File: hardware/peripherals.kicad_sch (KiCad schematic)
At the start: 40 parts, among them J2 Conn_FSR_TopRight, J3 Conn_FSR_BotRight, J4 Conn_FSR_TopLeft, J5 Conn_FSR_BotLeft, U2 BNO055, Y1 32.768k

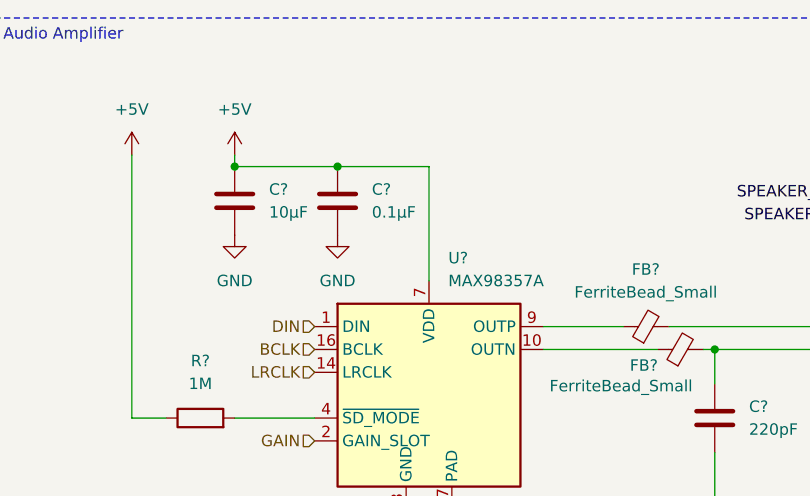
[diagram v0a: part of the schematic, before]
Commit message: Adding LED datasheet
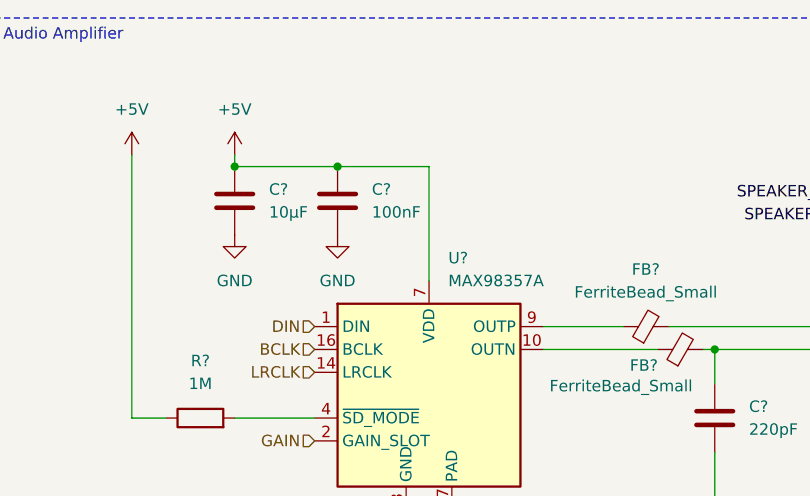
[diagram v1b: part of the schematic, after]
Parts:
- C?: value 0.1µF -> 100nF
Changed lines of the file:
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@@
 			)
 		)
-		(property "Value" "0.1µF"
+		(property "Value" "100nF"
 			(at 55.88 36.8299 0)
 			(effects
@@
 			)
 		)
-		(property "Datasheet" "https://cdn-shop.adafruit.com/product-files/1138/SK6812+LED+datasheet+.pdf"
+		(property "Datasheet" "https://github.com/Mowibox/chromapi_motherboard/blob/main/docs/datasheets/SK6812+LED+datasheet+.pdf"
 			(at 162.56 155.575 0)
 			(effects
@@
 			)
 		)
-		(property "Datasheet" "https://cdn-shop.adafruit.com/product-files/1138/SK6812+LED+datasheet+.pdf"
+		(property "Datasheet" "https://github.com/Mowibox/chromapi_motherboard/blob/main/docs/datasheets/SK6812+LED+datasheet+.pdf"
 			(at 162.56 120.015 0)
 			(effects

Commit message: Schematic first draft
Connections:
- net GAIN is gone; now on net GND: U?.2 (GAIN_SLOT)
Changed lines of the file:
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@@
 	(wire
 		(pts
+			(xy 49.53 62.23) (xy 48.26 62.23)
+		)
+		(stroke
+			(width 0)
+			(type default)
+		)
+	)
+	(wire
+		(pts
 			(xy 78.74 102.87) (xy 73.66 102.87)
 		)
@@
 	(wire
 		(pts
+			(xy 48.26 62.23) (xy 48.26 69.85)
+		)
+		(stroke
+			(width 0)
+			(type default)
+		)
+	)
+	(wire
+		(pts
 			(xy 199.39 97.79) (xy 199.39 102.87)
 		)
@@
 		)
 	)
-	(hierarchical_label "GAIN"
-		(shape input)
-		(at 49.53 62.23 180)
-		(effects
-			(font
-				(size 1.27 1.27)
-			)
-			(justify right)
-		)
-	)
 	(hierarchical_label "FSR_BotLeft"
 		(shape input)
@@
 					(unit 1)
 				)
+			)
+		)
+	)
+	(symbol
+		(lib_id "power:GND")
+		(at 48.26 69.85 0)
+		(unit 1)
+		(exclude_from_sim no)
+		(in_bom yes)
+		(on_board yes)
+		(dnp no)
+		(fields_autoplaced yes)
+		(property "Reference" "#PWR0105"
+			(at 48.26 76.2 0)
+			(effects
+				(font
+					(size 1.27 1.27)
+				)
+				(hide yes)
+			)
+		)
+		(property "Value" "GND"
+			(at 48.26 74.93 0)
+			(effects
+				(font
+					(size 1.27 1.27)
+				)
+			)
+		)
+		(property "Footprint" ""
+			(at 48.26 69.85 0)
+			(effects
+				(font
+					(size 1.27 1.27)
+				)
+				(hide yes)
+			)
+		)
+		(property "Datasheet" ""
+			(at 48.26 69.85 0)
+			(effects
+				(font
+					(size 1.27 1.27)
+				)
+				(hide yes)
+			)
+		)
+		(property "Description" "Power symbol creates a global label with name \"GND\" , ground"
+			(at 48.26 69.85 0)
+			(effects
+				(font
+					(size 1.27 1.27)
+				)
+				(hide yes)
+			)
+		)
+		(pin "1"
+		)
+		(instances
+			(project "chromapi_motherboard_v1"
+				(path "/d1a31f26-03e0-43e1-89c1-031fe31befc5/e7c408c3-7bc5-47c0-a90d-18a385ee9c4c"
+					(reference "#PWR0105")
+					(unit 1)
+				)

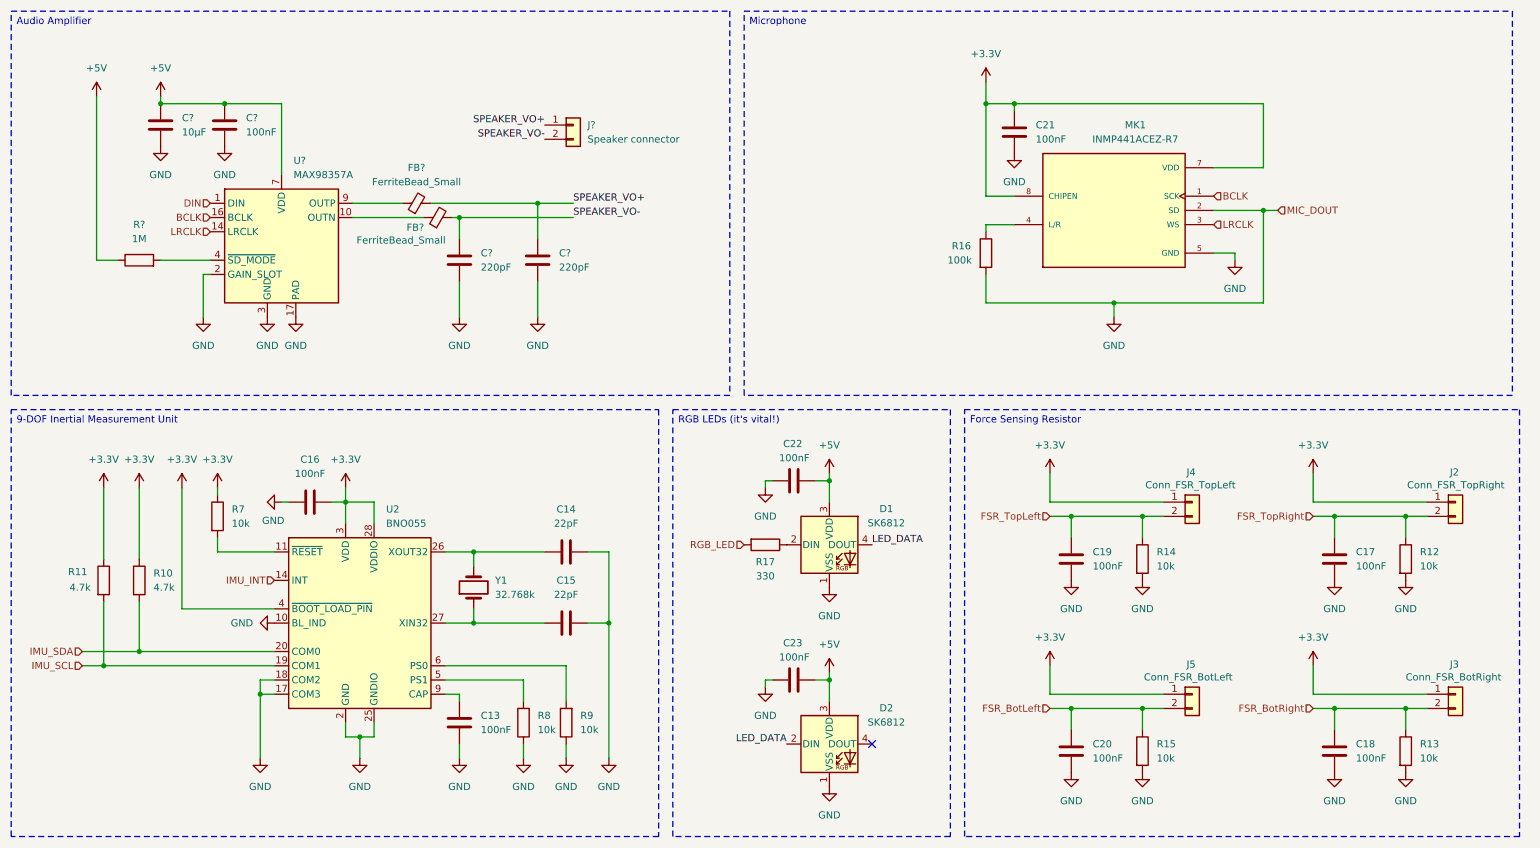
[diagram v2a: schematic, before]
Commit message: Annotating schematic
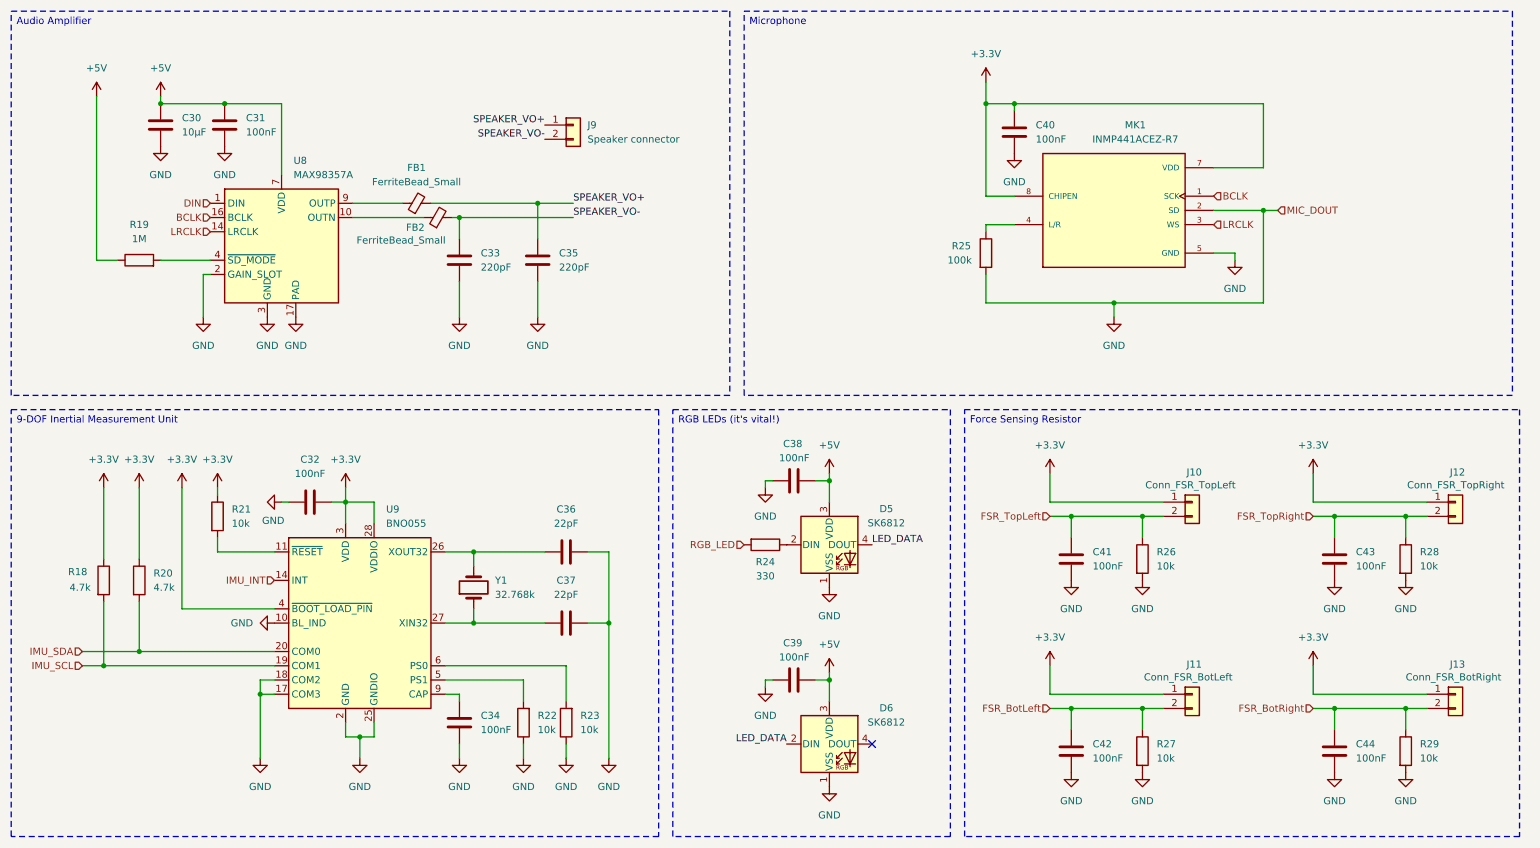
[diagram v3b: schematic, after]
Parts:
- gave numbers to parts that had none: 9
- renumbered C16 to C32, C13 to C34, C14 to C36, C15 to C37, C22 to C38, C23 to C39, C21 to C40, C19 to C41, C20 to C42, C17 to C43, C18 to C44, D1 to D5, D2 to D6, J4 to J10, J5 to J11, J2 to J12, J3 to J13, R11 to R18, R10 to R20, R7 to R21, R8 to R22, R9 to R23, R17 to R24, R16 to R25, R14 to R26, R15 to R27, R12 to R28, R13 to R29, U2 to U9

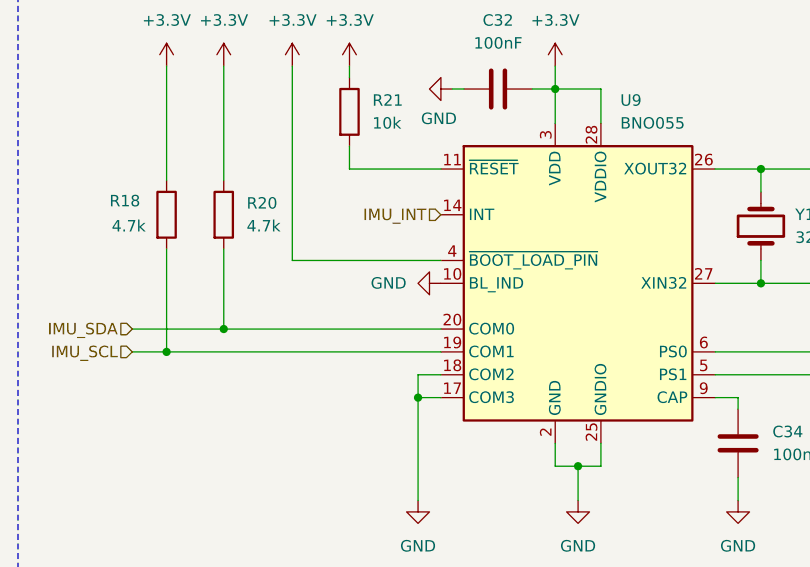
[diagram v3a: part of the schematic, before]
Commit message: Adding pwr flags
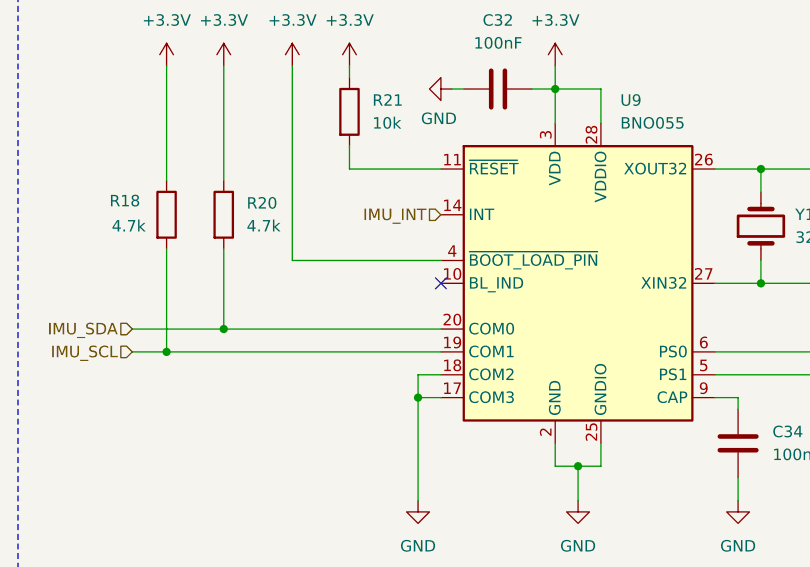
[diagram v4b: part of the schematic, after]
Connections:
- net GND: no longer U9.10 (BL_IND)
- no-connect marks 1 -> 2
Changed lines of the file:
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@@
 	)
 	(no_connect
+		(at 60.96 124.46)
+	)
+	(no_connect
 		(at 167.64 146.05)
 	)
@@
 					(unit 1)
 				)
-			)
-		)
-	)
-	(symbol
-		(lib_id "power:GND")
-		(at 60.96 124.46 270)
-		(unit 1)
-		(exclude_from_sim no)
-		(in_bom yes)
-		(on_board yes)
-		(dnp no)
-		(fields_autoplaced yes)
-		(property "Reference" "#PWR069"
-			(at 54.61 124.46 0)
-			(effects
-				(font
-					(size 1.27 1.27)
-				)
-				(hide yes)
-			)
-		)
-		(property "Value" "GND"
-			(at 57.15 124.4599 90)
-			(effects
-				(font
-					(size 1.27 1.27)
-				)
-				(justify right)
-			)
-		)
-		(property "Footprint" ""
-			(at 60.96 124.46 0)
-			(effects
-				(font
-					(size 1.27 1.27)
-				)
-				(hide yes)
-			)
-		)
-		(property "Datasheet" ""
-			(at 60.96 124.46 0)
-			(effects
-				(font
-					(size 1.27 1.27)
-				)
-				(hide yes)
-			)
-		)
-		(property "Description" "Power symbol creates a global label with name \"GND\" , ground"
-			(at 60.96 124.46 0)
-			(effects
-				(font
-					(size 1.27 1.27)
-				)
-				(hide yes)
-			)
-		)
-		(pin "1"
-		)
-		(instances
-			(project "chromapi_motherboard_v1"
-				(path "/d1a31f26-03e0-43e1-89c1-031fe31befc5/e7c408c3-7bc5-47c0-a90d-18a385ee9c4c"
-					(reference "#PWR069")
-					(unit 1)
-				)

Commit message: minor fixes
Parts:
- removed R25: 100k, symbol Device:R
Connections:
- net GND: now also MK1.4 (L/R)
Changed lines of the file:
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@@
 	(wire
 		(pts
-			(xy 187.96 62.23) (xy 187.96 67.31)
-		)
-		(stroke
-			(width 0)
-			(type default)
-		)
-	)
-	(wire
-		(pts
 			(xy 73.66 144.78) (xy 73.66 142.24)
 		)
@@
 	(wire
 		(pts
-			(xy 187.96 53.34) (xy 187.96 54.61)
+			(xy 187.96 53.34) (xy 187.96 67.31)
 		)
 		(stroke
@@
 					(unit 1)
 				)
-			)
-		)
-	)
-	(symbol
-		(lib_id "Device:R")
-		(at 187.96 58.42 0)
-		(unit 1)
-		(exclude_from_sim no)
-		(in_bom yes)
-		(on_board yes)
-		(dnp no)
-		(property "Reference" "R25"
-			(at 181.864 57.15 0)
-			(effects
-				(font
-					(size 1.27 1.27)
-				)
-				(justify left)
-			)
-		)
-		(property "Value" "100k"
-			(at 181.102 59.69 0)
-			(effects
-				(font
-					(size 1.27 1.27)
-				)
-				(justify left)
-			)
-		)
-		(property "Footprint" ""
-			(at 186.182 58.42 90)
-			(effects
-				(font
-					(size 1.27 1.27)
-				)
-				(hide yes)
-			)
-		)
-		(property "Datasheet" "~"
-			(at 187.96 58.42 0)
-			(effects
-				(font
-					(size 1.27 1.27)
-				)
-				(hide yes)
-			)
-		)
-		(property "Description" "Resistor"
-			(at 187.96 58.42 0)
-			(effects
-				(font
-					(size 1.27 1.27)
-				)
-				(hide yes)
-			)
-		)
-		(pin "2"
-		)
-		(pin "1"
-		)
-		(instances
-			(project "chromapi_motherboard_v1"
-				(path "/d1a31f26-03e0-43e1-89c1-031fe31befc5/e7c408c3-7bc5-47c0-a90d-18a385ee9c4c"
-					(reference "R25")
-					(unit 1)
-				)

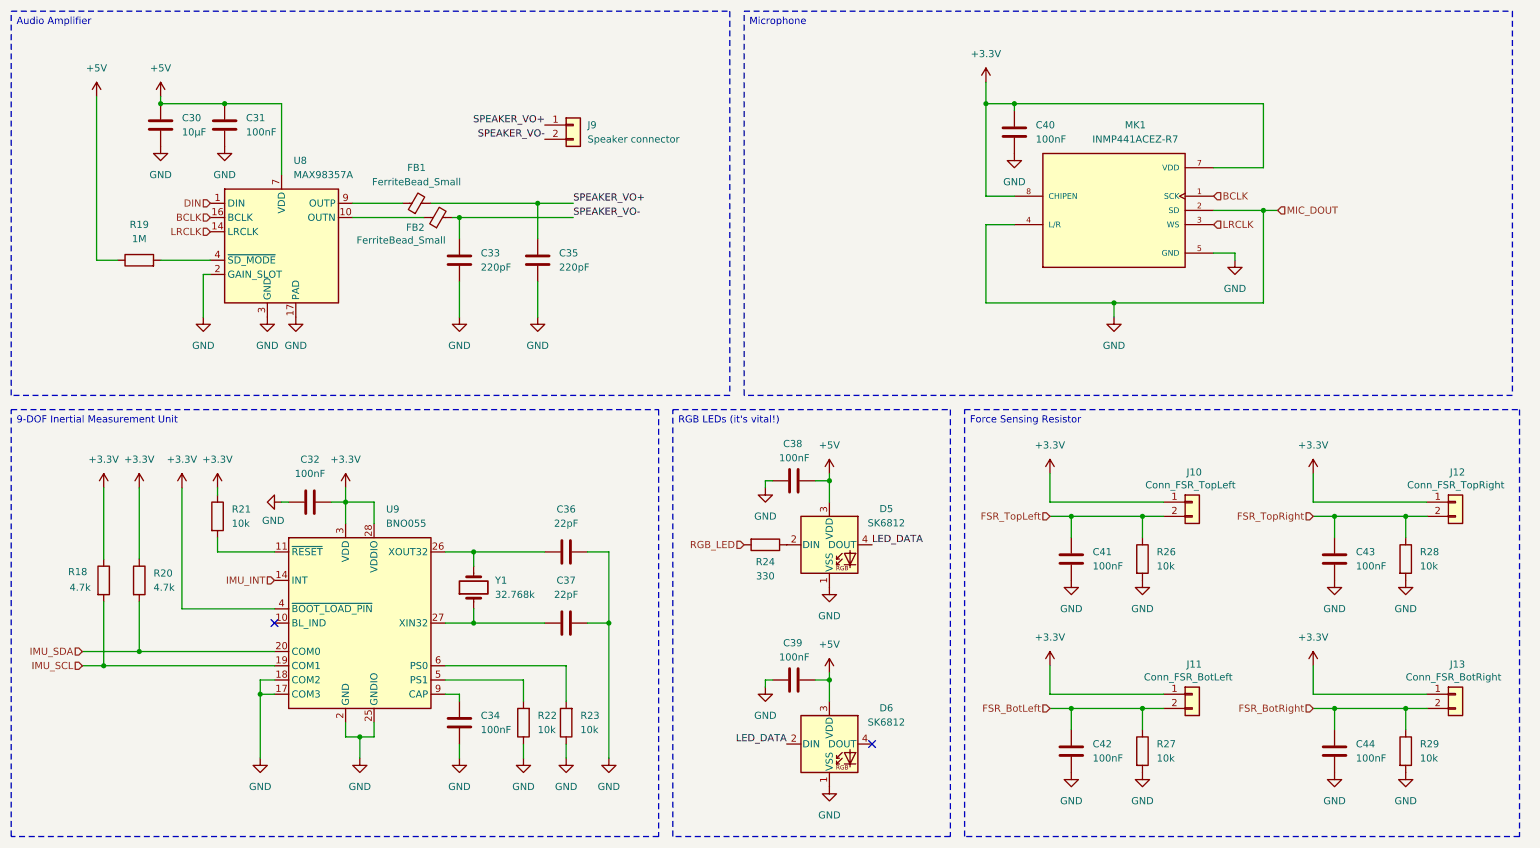
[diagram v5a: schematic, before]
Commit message: Adding test points
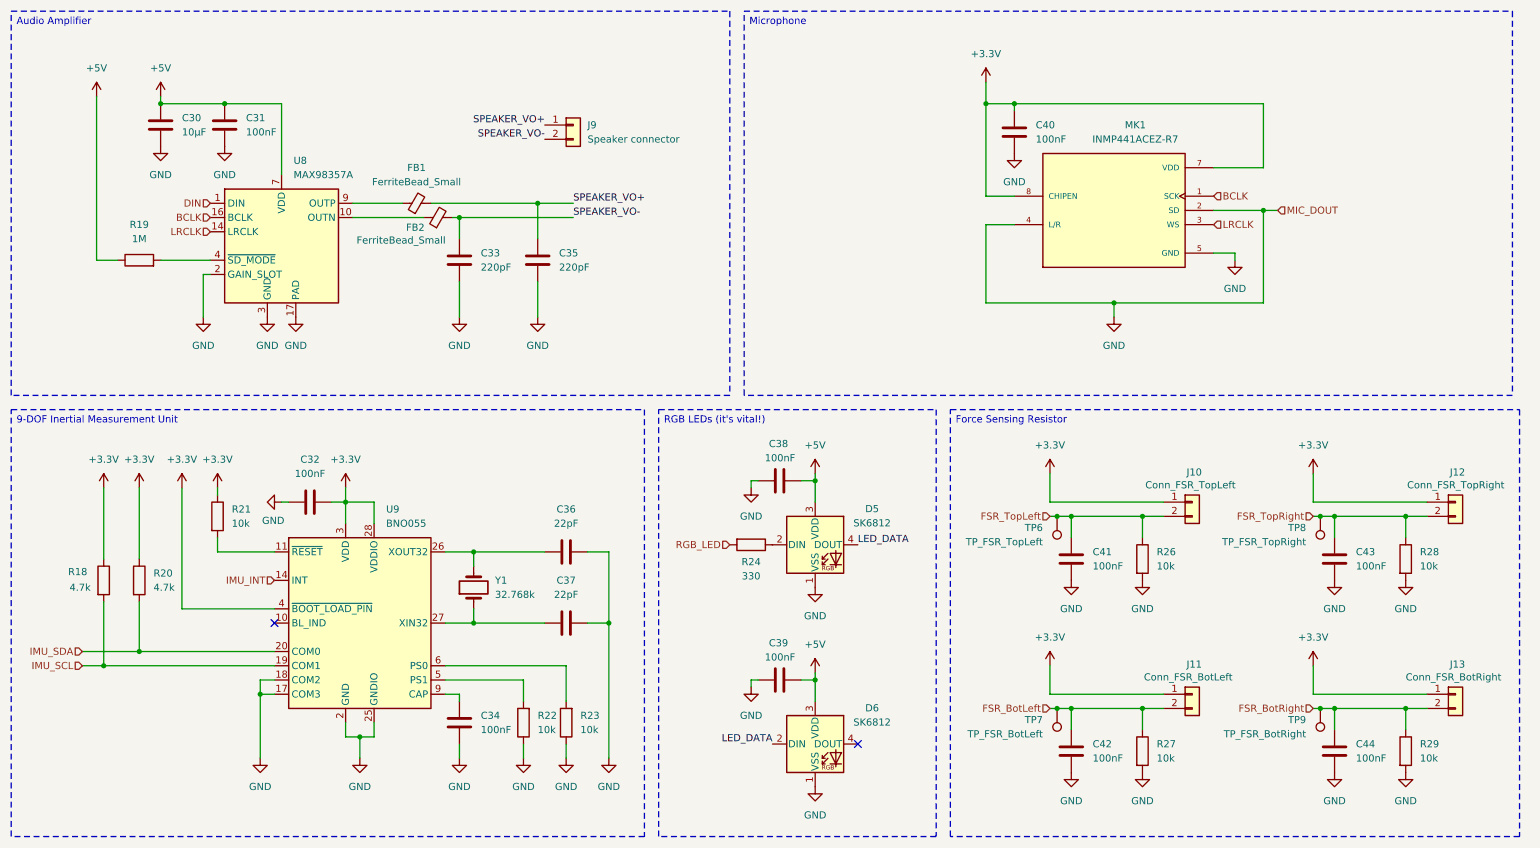
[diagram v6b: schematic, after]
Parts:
- added TP6: TP_FSR_TopLeft, symbol Connector:TestPoint
- added TP7: TP_FSR_BotLeft, symbol Connector:TestPoint
- added TP8: TP_FSR_TopRight, symbol Connector:TestPoint
- added TP9: TP_FSR_BotRight, symbol Connector:TestPoint
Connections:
- net FSR_BotLeft: now also TP7.1
- net FSR_BotRight: now also TP9.1
- net FSR_TopLeft: now also TP6.1
- net FSR_TopRight: now also TP8.1
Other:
- moved on the sheet: C38, C39, D5, D6, R24

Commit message: Annotating components
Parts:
- renumbered R26 to R25, R27 to R26, R28 to R27, R29 to R28, TP8 to TP10, TP9 to TP11, TP6 to TP8, TP7 to TP9
